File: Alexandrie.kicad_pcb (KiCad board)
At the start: 2 copper layers, 100 x 100 mm, 786 parts, among them J1 kk_10, J11 CONN_01X03, J2 kk_5, J3 kk_5, J4 CONN_01X06, J5 CONN_01X02, J6 CONN_01X13, J7 Conn_01x07, J8 kk_10, U1 74HCT04, U12 78M05 Dpak, U2 74HCT04, U3 TPIC6B595, U4 TPIC6B595, U6 TPIC6B595, U7 TPIC6B595

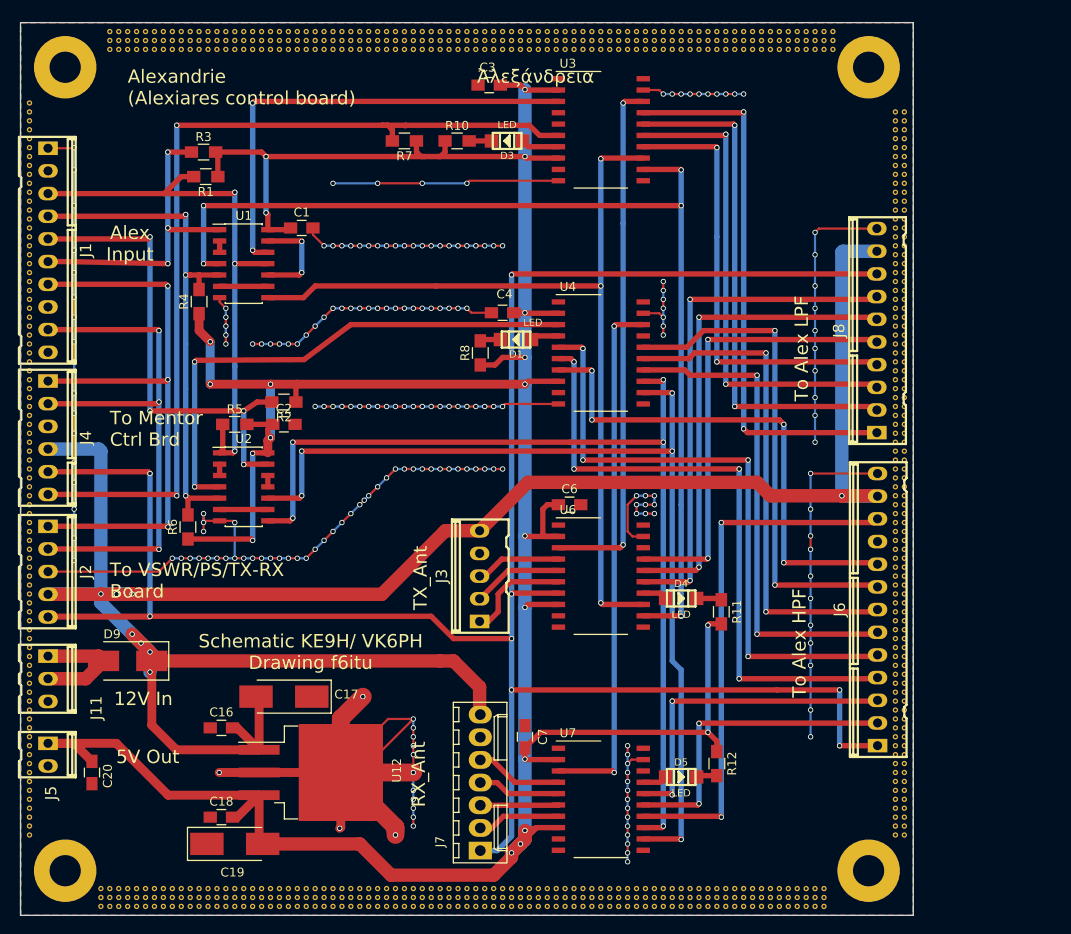
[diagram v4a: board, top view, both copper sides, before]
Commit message: upgrate to Kicad 5.0n, new up to date Gerber
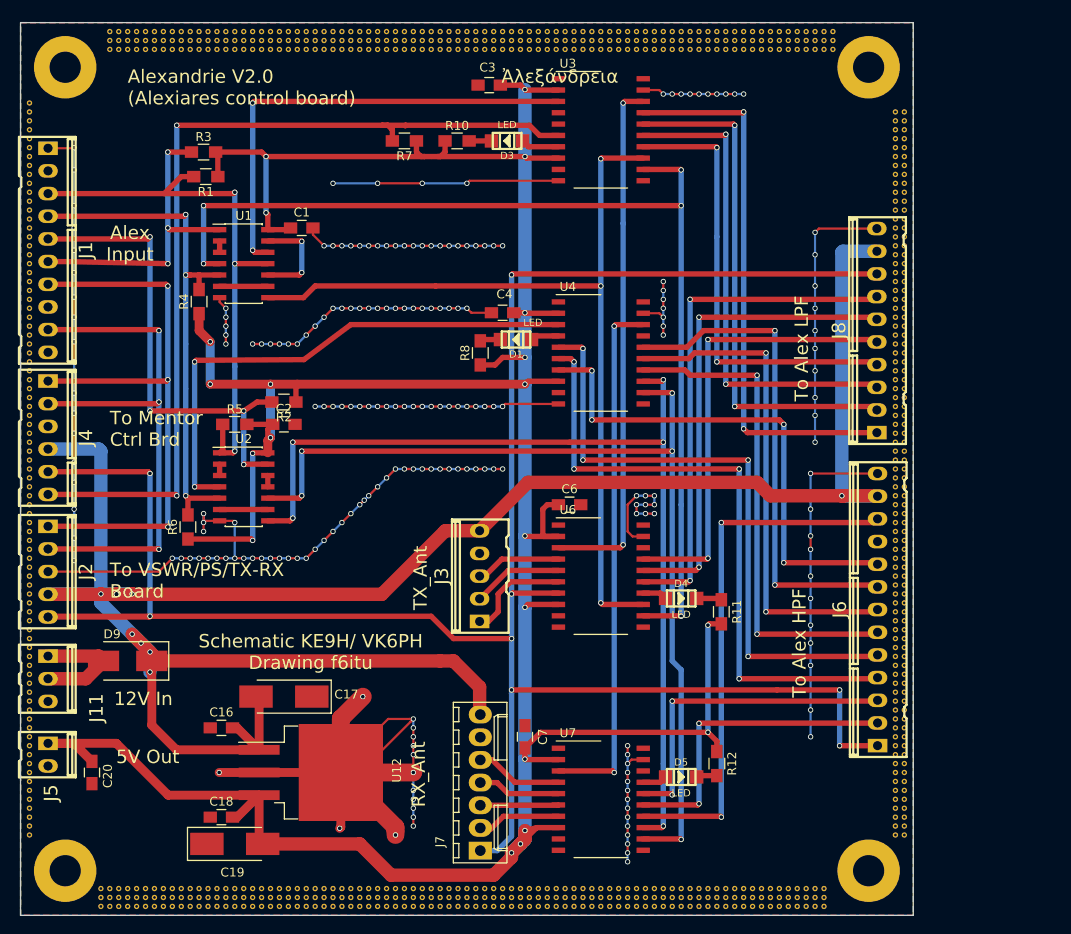
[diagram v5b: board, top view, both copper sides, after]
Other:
- board text added: "Alexandrie V2.0 Ἀλεξάνδρεια (Alexiares control board)"
- board text removed: "Alexandrie Ἀλεξάνδρεια (Alexiares control board)"
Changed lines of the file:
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@@
-(kicad_pcb (version 4) (host pcbnew 4.0.7)
+(kicad_pcb (version 20171130) (host pcbnew "(5.0.2)-1")
   (general
-    (links 902)
-    (no_connects 0)
-    (area 88.924999 42.924999 189.075001 143.075001)
     (thickness 1.6)
     (drawings 27)
@@
     (pad_drill 0.3)
     (pad_to_mask_clearance 0.2)
+    (solder_mask_min_width 0.25)
     (aux_axis_origin 0 0)
     (visible_elements 7FFFF77F)
     (pcbplotparams
-      (layerselection 0x010f0_80000001)
+      (layerselection 0x010f0_ffffffff)
       (usegerberextensions true)
-      (excludeedgelayer true)
+      (usegerberattributes true)
+      (usegerberadvancedattributes false)
+      (creategerberjobfile false)
+      (excludeedgelayer false)
       (linewidth 0.100000)
       (plotframeref false)
@@
       (hpglpennumber 1)
       (hpglpenspeed 20)
-      (hpglpendiameter 15)
-      (hpglpenoverlay 2)
+      (hpglpendiameter 15.000000)
       (psnegative false)
       (psa4output false)
@@
       (drillshape 0)
       (scaleselection 1)
-      (outputdirectory Gerber/))
+      (outputdirectory "Gerber/"))
   )
   (net 0 "")
@@
     (descr "10 pin vert. connector, Molex KK100 series")
     (fp_text reference J1 (at 0 -4.318 270) (layer F.SilkS)
-      (effects (font (thickness 0.3048)))
+      (effects (font (size 1.524 1.524) (thickness 0.3048)))
     )
     (fp_text value kk_10 (at 0 4.56946 270) (layer F.SilkS) hide
-      (effects (font (thickness 0.3048)))
+      (effects (font (size 1.524 1.524) (thickness 0.3048)))
     )
     (fp_line (start -2.286 -2.286) (end 12.446 -2.286) (layer F.SilkS) (width 0.254))
@@
     (descr "5 pin vert. connector, Molex KK100 series")
     (fp_text reference J2 (at 0 -4.318 270) (layer F.SilkS)
-      (effects (font (thickness 0.3048)))
+      (effects (font (size 1.524 1.524) (thickness 0.3048)))
     )
     (fp_text value kk_5 (at 0 4.56946 270) (layer F.SilkS) hide
-      (effects (font (thickness 0.3048)))
+      (effects (font (size 1.524 1.524) (thickness 0.3048)))
     )
     (fp_line (start 6.096 -2.794) (end -6.096 -2.794) (layer F.SilkS) (width 0.254))
@@
     (descr "6 pin vert. connector, Molex KK100 series")
     (fp_text reference J4 (at 0 -4.318 270) (layer F.SilkS)
-      (effects (font (thickness 0.3048)))
+      (effects (font (size 1.524 1.524) (thickness 0.3048)))
     )
     (fp_text value CONN_01X06 (at 0 4.56946 270) (layer F.SilkS) hide
-      (effects (font (thickness 0.3048)))
+      (effects (font (size 1.524 1.524) (thickness 0.3048)))
     )
     (fp_line (start 2.794 -2.286) (end 7.366 -2.286) (layer F.SilkS) (width 0.254))
@@
     (descr "2 pin vert. connector, Molex KK100 series")
     (fp_text reference J5 (at 4.3 -0.415 270) (layer F.SilkS)
-      (effects (font (thickness 0.3048)))
+      (effects (font (size 1.524 1.524) (thickness 0.3048)))
     )
     (fp_text value CONN_01X02 (at 0 4.572 270) (layer F.SilkS) hide
-      (effects (font (thickness 0.3048)))
+      (effects (font (size 1.524 1.524) (thickness 0.3048)))
     )
     (fp_line (start -2.286 -2.286) (end 2.286 -2.286) (layer F.SilkS) (width 0.254))
@@
     (descr "10 pin vert. connector, Molex KK100 series")
     (fp_text reference J8 (at 0 -4.318 90) (layer F.SilkS)
-      (effects (font (thickness 0.3048)))
+      (effects (font (size 1.524 1.524) (thickness 0.3048)))
     )
     (fp_text value kk_10 (at 0 4.56946 90) (layer F.SilkS) hide
-      (effects (font (thickness 0.3048)))
+      (effects (font (size 1.524 1.524) (thickness 0.3048)))
     )
     (fp_line (start -2.286 -2.286) (end 12.446 -2.286) (layer F.SilkS) (width 0.254))
@@
     (descr "3 pin vert. connector, Molex KK100 series")
     (fp_text reference J11 (at 3.275 -5.495 270) (layer F.SilkS)
-      (effects (font (thickness 0.3048)))
+      (effects (font (size 1.524 1.524) (thickness 0.3048)))
     )
     (fp_text value CONN_01X03 (at 0 4.56946 270) (layer F.SilkS) hide
-      (effects (font (thickness 0.3048)))
+      (effects (font (size 1.524 1.524) (thickness 0.3048)))
     )
     (fp_line (start -3.556 -2.286) (end 3.556 -2.286) (layer F.SilkS) (width 0.254))
@@
       (net 2 GND))
     (model TO_SOT_Packages_SMD.3dshapes/TO-263-3Lead.wrl
-      (at (xyz -0.2 0 0))
+      (offset (xyz -5.079999923706055 0 0))
       (scale (xyz 1 1 1))
       (rotate (xyz 0 0 90))
@@
     (descr "5 pin vert. connector, Molex KK100 series")
     (fp_text reference J3 (at 0 -4.318 90) (layer F.SilkS)
-      (effects (font (thickness 0.3048)))
+      (effects (font (size 1.524 1.524) (thickness 0.3048)))
     )
     (fp_text value kk_5 (at 0 4.56946 90) (layer F.SilkS) hide
-      (effects (font (thickness 0.3048)))
+      (effects (font (size 1.524 1.524) (thickness 0.3048)))
     )
     (fp_line (start 6.096 -2.794) (end -6.096 -2.794) (layer F.SilkS) (width 0.254))
@@
     (descr "13 pin vert. connector, Molex KK100 series")
     (fp_text reference J6 (at 0 -4.318 90) (layer F.SilkS)
-      (effects (font (thickness 0.3048)))
+      (effects (font (size 1.524 1.524) (thickness 0.3048)))
     )
     (fp_text value CONN_01X13 (at 0 4.56946 90) (layer F.SilkS) hide
-      (effects (font (thickness 0.3048)))
+      (effects (font (size 1.524 1.524) (thickness 0.3048)))
     )
     (fp_line (start 4.064 -2.794) (end 16.256 -2.794) (layer F.SilkS) (width 0.254))
@@
       (net 18 +12V))
     (model ${KISYS3DMOD}/Connectors_Molex.3dshapes/Molex_KK-6410-07_07x2.54mm_Straight.wrl
-      (at (xyz 0.6 0 0))
+      (offset (xyz 15.23999977111816 0 0))
       (scale (xyz 1 1 1))
       (rotate (xyz 0 0 180))
@@
     (effects (font (size 1.5 1.5) (thickness 0.3)) (justify left mirror))
   )
-  (gr_text "Alexandrie                                           Ἀλεξάνδρεια \n(Alexiares control board)\n" (at 101 50.25) (layer F.SilkS)
+  (gr_text "Alexandrie V2.0                                       Ἀλεξάνδρεια \n(Alexiares control board)\n" (at 101 50.25) (layer F.SilkS)
     (effects (font (size 1.5 1.5) (thickness 0.3)) (justify left))
   )

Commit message: cleaning, new bom and interactive bom
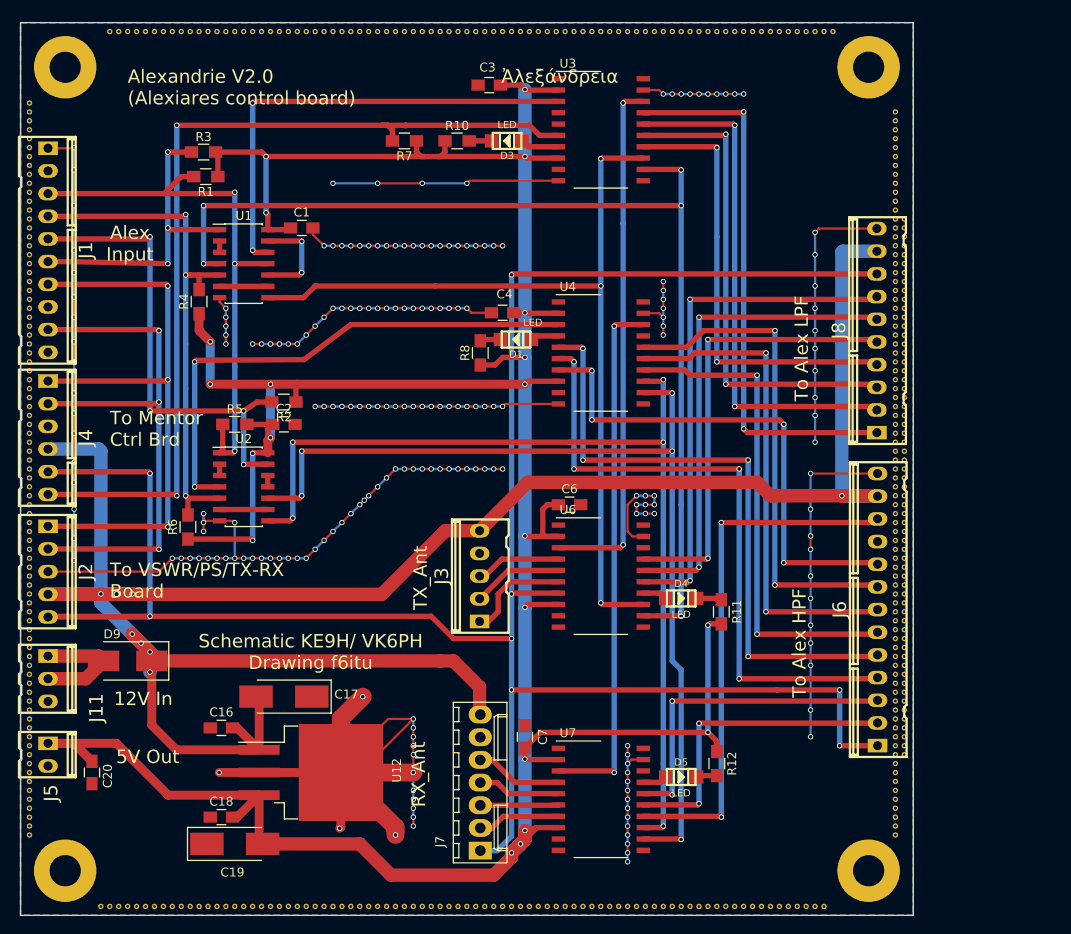
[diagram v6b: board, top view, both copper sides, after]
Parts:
- removed the REF** at (179.0, 141.0)
- removed the REF** at (178.0, 141.0)
- removed the REF** at (177.0, 141.0)
- removed the REF** at (176.0, 141.0)
- removed the REF** at (175.0, 141.0)
- removed the REF** at (174.0, 141.0)
- removed the REF** at (173.0, 141.0)
- removed the REF** at (172.0, 141.0)
- removed the REF** at (171.0, 141.0)
- removed the REF** at (170.0, 141.0)
- removed the REF** at (169.0, 141.0)
- removed the REF** at (168.0, 141.0)
- removed the REF** at (167.0, 141.0)
- removed the REF** at (166.0, 141.0)
- removed the REF** at (165.0, 141.0)
- removed the REF** at (164.0, 141.0)
- removed the REF** at (163.0, 141.0)
- removed the REF** at (162.0, 141.0)
- removed the REF** at (161.0, 141.0)
- removed the REF** at (160.0, 141.0)
- removed the REF** at (159.0, 141.0)
- removed the REF** at (158.0, 141.0)
- removed the REF** at (157.0, 141.0)
- removed the REF** at (156.0, 141.0)
- removed the REF** at (155.0, 141.0)
- removed the REF** at (154.0, 141.0)
- removed the REF** at (153.0, 141.0)
- removed the REF** at (152.0, 141.0)
- removed the REF** at (151.0, 141.0)
- removed the REF** at (150.0, 141.0)
- removed the REF** at (149.0, 141.0)
- removed the REF** at (148.0, 141.0)
- removed the REF** at (147.0, 141.0)
- removed the REF** at (146.0, 141.0)
- removed the REF** at (145.0, 141.0)
- removed the REF** at (144.0, 141.0)
- removed the REF** at (143.0, 141.0)
- removed the REF** at (142.0, 141.0)
- removed the REF** at (141.0, 141.0)
- removed the REF** at (140.0, 141.0)
- removed the REF** at (139.0, 141.0)
- removed the REF** at (138.0, 141.0)
- removed the REF** at (137.0, 141.0)
- removed the REF** at (136.0, 141.0)
- removed the REF** at (135.0, 141.0)
- removed the REF** at (134.0, 141.0)
- removed the REF** at (133.0, 141.0)
- removed the REF** at (132.0, 141.0)
- removed the REF** at (131.0, 141.0)
- removed the REF** at (130.0, 141.0)
- removed the REF** at (129.0, 141.0)
- removed the REF** at (128.0, 141.0)
- removed the REF** at (127.0, 141.0)
- removed the REF** at (126.0, 141.0)
- removed the REF** at (125.0, 141.0)
- removed the REF** at (124.0, 141.0)
- removed the REF** at (123.0, 141.0)
- removed the REF** at (122.0, 141.0)
- removed the REF** at (121.0, 141.0)
- removed the REF** at (120.0, 141.0)
- removed the REF** at (119.0, 141.0)
- removed the REF** at (118.0, 141.0)
- removed the REF** at (117.0, 141.0)
- removed the REF** at (116.0, 141.0)
- removed the REF** at (115.0, 141.0)
- removed the REF** at (114.0, 141.0)
- removed the REF** at (113.0, 141.0)
- removed the REF** at (112.0, 141.0)
- removed the REF** at (111.0, 141.0)
- removed the REF** at (110.0, 141.0)
- removed the REF** at (109.0, 141.0)
- removed the REF** at (108.0, 141.0)
- removed the REF** at (107.0, 141.0)
- removed the REF** at (106.0, 141.0)
- removed the REF** at (105.0, 141.0)
- removed the REF** at (104.0, 141.0)
- removed the REF** at (103.0, 141.0)
- removed the REF** at (102.0, 141.0)
- removed the REF** at (101.0, 141.0)
- removed the REF** at (100.0, 141.0)
- removed the REF** at (99.0, 141.0)
- removed the REF** at (98.0, 141.0)
- removed the REF** at (179.0, 140.0)
- removed the REF** at (178.0, 140.0)
- removed the REF** at (177.0, 140.0)
- removed the REF** at (176.0, 140.0)
- removed the REF** at (175.0, 140.0)
- removed the REF** at (174.0, 140.0)
- removed the REF** at (173.0, 140.0)
- removed the REF** at (172.0, 140.0)
- removed the REF** at (171.0, 140.0)
- removed the REF** at (170.0, 140.0)
- removed the REF** at (169.0, 140.0)
- removed the REF** at (168.0, 140.0)
- removed the REF** at (167.0, 140.0)
- removed the REF** at (166.0, 140.0)
- removed the REF** at (165.0, 140.0)
- removed the REF** at (164.0, 140.0)
- removed the REF** at (163.0, 140.0)
- removed the REF** at (162.0, 140.0)
- removed the REF** at (161.0, 140.0)
- removed the REF** at (160.0, 140.0)
- removed the REF** at (159.0, 140.0)
- removed the REF** at (158.0, 140.0)
- removed the REF** at (157.0, 140.0)
- removed the REF** at (156.0, 140.0)
- removed the REF** at (155.0, 140.0)
- removed the REF** at (154.0, 140.0)
- removed the REF** at (153.0, 140.0)
- removed the REF** at (152.0, 140.0)
- removed the REF** at (151.0, 140.0)
- removed the REF** at (150.0, 140.0)
- removed the REF** at (149.0, 140.0)
- removed the REF** at (148.0, 140.0)
- removed the REF** at (147.0, 140.0)
- removed the REF** at (146.0, 140.0)
- removed the REF** at (145.0, 140.0)
- removed the REF** at (144.0, 140.0)
- removed the REF** at (143.0, 140.0)
- removed the REF** at (142.0, 140.0)
- removed the REF** at (141.0, 140.0)
- removed the REF** at (140.0, 140.0)
- removed the REF** at (139.0, 140.0)
- removed the REF** at (138.0, 140.0)
- removed the REF** at (137.0, 140.0)
- removed the REF** at (136.0, 140.0)
- removed the REF** at (135.0, 140.0)
- removed the REF** at (134.0, 140.0)
- removed the REF** at (133.0, 140.0)
- removed the REF** at (132.0, 140.0)
- removed the REF** at (131.0, 140.0)
- removed the REF** at (130.0, 140.0)
- removed the REF** at (129.0, 140.0)
- removed the REF** at (128.0, 140.0)
- removed the REF** at (127.0, 140.0)
- removed the REF** at (126.0, 140.0)
- removed the REF** at (125.0, 140.0)
- removed the REF** at (124.0, 140.0)
- removed the REF** at (123.0, 140.0)
- removed the REF** at (122.0, 140.0)
- removed the REF** at (121.0, 140.0)
- removed the REF** at (120.0, 140.0)
- removed the REF** at (119.0, 140.0)
- removed the REF** at (118.0, 140.0)
- removed the REF** at (117.0, 140.0)
- removed the REF** at (116.0, 140.0)
- removed the REF** at (115.0, 140.0)
- removed the REF** at (114.0, 140.0)
- removed the REF** at (113.0, 140.0)
- removed the REF** at (112.0, 140.0)
- removed the REF** at (111.0, 140.0)
- removed the REF** at (110.0, 140.0)
- removed the REF** at (109.0, 140.0)
- removed the REF** at (108.0, 140.0)
- removed the REF** at (107.0, 140.0)
- removed the REF** at (106.0, 140.0)
- removed the REF** at (105.0, 140.0)
- removed the REF** at (104.0, 140.0)
- removed the REF** at (103.0, 140.0)
- removed the REF** at (102.0, 140.0)
- removed the REF** at (101.0, 140.0)
- removed the REF** at (100.0, 140.0)
- removed the REF** at (99.0, 140.0)
- removed the REF** at (98.0, 140.0)
- removed the REF** at (188.0, 134.0)
- removed the REF** at (188.0, 133.0)
- removed the REF** at (188.0, 132.0)
- removed the REF** at (188.0, 131.0)
- removed the REF** at (188.0, 130.0)
- removed the REF** at (188.0, 129.0)
- removed the REF** at (188.0, 128.0)
- removed the REF** at (188.0, 127.0)
- removed the REF** at (188.0, 126.0)
- removed the REF** at (188.0, 64.0)
- removed the REF** at (188.0, 63.0)
- removed the REF** at (188.0, 62.0)
- removed the REF** at (188.0, 61.0)
- removed the REF** at (188.0, 60.0)
- removed the REF** at (188.0, 59.0)
- removed the REF** at (188.0, 58.0)
- removed the REF** at (188.0, 57.0)
- removed the REF** at (188.0, 56.0)
- removed the REF** at (188.0, 55.0)
- removed the REF** at (188.0, 54.0)
- removed the REF** at (188.0, 53.0)
- removed the REF** at (180.0, 46.0)
- removed the REF** at (179.0, 46.0)
- removed the REF** at (178.0, 46.0)
- removed the REF** at (177.0, 46.0)
- removed the REF** at (176.0, 46.0)
- removed the REF** at (175.0, 46.0)
- removed the REF** at (174.0, 46.0)
- removed the REF** at (173.0, 46.0)
- removed the REF** at (172.0, 46.0)
- removed the REF** at (171.0, 46.0)
- removed the REF** at (170.0, 46.0)
- removed the REF** at (169.0, 46.0)
- removed the REF** at (168.0, 46.0)
- removed the REF** at (167.0, 46.0)
- removed the REF** at (166.0, 46.0)
- removed the REF** at (165.0, 46.0)
- removed the REF** at (164.0, 46.0)
- removed the REF** at (163.0, 46.0)
- removed the REF** at (162.0, 46.0)
- removed the REF** at (161.0, 46.0)
- removed the REF** at (160.0, 46.0)
- removed the REF** at (159.0, 46.0)
- removed the REF** at (158.0, 46.0)
- removed the REF** at (157.0, 46.0)
- removed the REF** at (156.0, 46.0)
- removed the REF** at (155.0, 46.0)
- removed the REF** at (154.0, 46.0)
- removed the REF** at (153.0, 46.0)
- removed the REF** at (152.0, 46.0)
- removed the REF** at (151.0, 46.0)
- removed the REF** at (150.0, 46.0)
- removed the REF** at (149.0, 46.0)
- removed the REF** at (148.0, 46.0)
- removed the REF** at (147.0, 46.0)
- removed the REF** at (146.0, 46.0)
- removed the REF** at (145.0, 46.0)
- removed the REF** at (144.0, 46.0)
- removed the REF** at (143.0, 46.0)
- removed the REF** at (142.0, 46.0)
- removed the REF** at (141.0, 46.0)
- removed the REF** at (140.0, 46.0)
- removed the REF** at (139.0, 46.0)
- removed the REF** at (138.0, 46.0)
- removed the REF** at (137.0, 46.0)
- removed the REF** at (136.0, 46.0)
- removed the REF** at (135.0, 46.0)
- removed the REF** at (134.0, 46.0)
- removed the REF** at (133.0, 46.0)
- removed the REF** at (132.0, 46.0)
- removed the REF** at (131.0, 46.0)
- removed the REF** at (130.0, 46.0)
- removed the REF** at (129.0, 46.0)
- removed the REF** at (128.0, 46.0)
- removed the REF** at (127.0, 46.0)
- removed the REF** at (126.0, 46.0)
- removed the REF** at (125.0, 46.0)
- removed the REF** at (124.0, 46.0)
- removed the REF** at (123.0, 46.0)
- removed the REF** at (122.0, 46.0)
- removed the REF** at (121.0, 46.0)
- removed the REF** at (120.0, 46.0)
- removed the REF** at (119.0, 46.0)
- removed the REF** at (118.0, 46.0)
- removed the REF** at (117.0, 46.0)
- removed the REF** at (116.0, 46.0)
- removed the REF** at (115.0, 46.0)
- removed the REF** at (114.0, 46.0)
- removed the REF** at (113.0, 46.0)
- removed the REF** at (112.0, 46.0)
- removed the REF** at (111.0, 46.0)
- removed the REF** at (110.0, 46.0)
- removed the REF** at (109.0, 46.0)
- removed the REF** at (108.0, 46.0)
- removed the REF** at (107.0, 46.0)
- removed the REF** at (106.0, 46.0)
- removed the REF** at (105.0, 46.0)
- removed the REF** at (104.0, 46.0)
- removed the REF** at (103.0, 46.0)
- removed the REF** at (102.0, 46.0)
- removed the REF** at (101.0, 46.0)
- removed the REF** at (100.0, 46.0)
- removed the REF** at (99.0, 46.0)
- removed the REF** at (180.0, 45.0)
- removed the REF** at (179.0, 45.0)
- removed the REF** at (178.0, 45.0)
- removed the REF** at (177.0, 45.0)
- removed the REF** at (176.0, 45.0)
- removed the REF** at (175.0, 45.0)
- removed the REF** at (174.0, 45.0)
- removed the REF** at (173.0, 45.0)
- removed the REF** at (172.0, 45.0)
- removed the REF** at (171.0, 45.0)
- removed the REF** at (170.0, 45.0)
- removed the REF** at (169.0, 45.0)
- removed the REF** at (168.0, 45.0)
- removed the REF** at (167.0, 45.0)
- removed the REF** at (166.0, 45.0)
- removed the REF** at (165.0, 45.0)
- removed the REF** at (164.0, 45.0)
- removed the REF** at (163.0, 45.0)
- removed the REF** at (162.0, 45.0)
- removed the REF** at (161.0, 45.0)
- removed the REF** at (160.0, 45.0)
- removed the REF** at (159.0, 45.0)
- removed the REF** at (158.0, 45.0)
- removed the REF** at (157.0, 45.0)
- removed the REF** at (156.0, 45.0)
- removed the REF** at (155.0, 45.0)
- removed the REF** at (154.0, 45.0)
- removed the REF** at (153.0, 45.0)
- removed the REF** at (152.0, 45.0)
- removed the REF** at (151.0, 45.0)
- removed the REF** at (150.0, 45.0)
- removed the REF** at (149.0, 45.0)
- removed the REF** at (148.0, 45.0)
- removed the REF** at (147.0, 45.0)
- removed the REF** at (146.0, 45.0)
- removed the REF** at (145.0, 45.0)
- removed the REF** at (144.0, 45.0)
- removed the REF** at (143.0, 45.0)
- removed the REF** at (142.0, 45.0)
- removed the REF** at (141.0, 45.0)
- removed the REF** at (140.0, 45.0)
- removed the REF** at (139.0, 45.0)
- removed the REF** at (138.0, 45.0)
- removed the REF** at (137.0, 45.0)
- removed the REF** at (136.0, 45.0)
- removed the REF** at (135.0, 45.0)
- removed the REF** at (134.0, 45.0)
- removed the REF** at (133.0, 45.0)
- removed the REF** at (132.0, 45.0)
- removed the REF** at (131.0, 45.0)
- removed the REF** at (130.0, 45.0)
- removed the REF** at (129.0, 45.0)
- removed the REF** at (128.0, 45.0)
- removed the REF** at (127.0, 45.0)
- removed the REF** at (126.0, 45.0)
- removed the REF** at (125.0, 45.0)
- removed the REF** at (124.0, 45.0)
- removed the REF** at (123.0, 45.0)
- removed the REF** at (122.0, 45.0)
- removed the REF** at (121.0, 45.0)
- removed the REF** at (120.0, 45.0)
- removed the REF** at (119.0, 45.0)
- removed the REF** at (118.0, 45.0)
- removed the REF** at (117.0, 45.0)
- removed the REF** at (116.0, 45.0)
- removed the REF** at (115.0, 45.0)
- removed the REF** at (114.0, 45.0)
- removed the REF** at (113.0, 45.0)
- removed the REF** at (112.0, 45.0)
- removed the REF** at (111.0, 45.0)
- removed the REF** at (110.0, 45.0)
- removed the REF** at (109.0, 45.0)
- removed the REF** at (108.0, 45.0)
- removed the REF** at (107.0, 45.0)
- removed the REF** at (106.0, 45.0)
- removed the REF** at (105.0, 45.0)
- removed the REF** at (104.0, 45.0)
- removed the REF** at (103.0, 45.0)
- removed the REF** at (102.0, 45.0)
- removed the REF** at (101.0, 45.0)
- removed the REF** at (100.0, 45.0)
- removed the REF** at (99.0, 45.0)

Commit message: last commit, project deprecated, replaced by AlexV2
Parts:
- removed REF** (x390): via, via:via
- C1, C16, C18, C2, C20, C3, C4, C6, C7: footprint Capacitors_SMD:C_0805_HandSoldering -> Capacitor_SMD:C_0805_2012Metric_Pad1.18x1.45mm_HandSolder
- D1, D3, D4, D5: footprint smd_leds:Led_1206 -> LED_SMD:LED_1206_3216Metric_Pad1.42x1.75mm_HandSolder
- R1, R10, R11, R12, R2, R3, R4, R5, R6, R7, R8: footprint Resistors_SMD:R_0805_HandSoldering -> Resistor_SMD:R_0805_2012Metric_Pad1.20x1.40mm_HandSolder
- U1, U2: footprint Housings_SOIC:SOIC-14_3.9x8.7mm_Pitch1.27mm -> Package_SO:SO-14_3.9x8.65mm_P1.27mm
- U3, U4, U6, U7: footprint Housings_SOIC:SO-20_12.8x7.5mm_Pitch1.27mm -> Package_SO:SO-20_12.8x7.5mm_P1.27mm
- turned C17 to 0 degrees
- turned C19 to 180 degrees
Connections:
- net 12/10m renamed 12/10m
- net 17/15m renamed 17/15m
- net 30/20m renamed 30/20m
- C17 pad 1: GND -> +12V
- C17 pad 2: +12V -> GND
- C19 pad 1: GND -> +5V
- C19 pad 2: +5V -> GND
- J1 pad 2: (no net) -> unconnected-(J1-Pad2)
- J1 pad 8: (no net) -> unconnected-(J1-Pad8)
- U3 pad 1: (no net) -> unconnected-(U3-Pad1)
- U3 pad 20: (no net) -> unconnected-(U3-Pad20)
- U3 pad 4: (no net) -> unconnected-(U3-Pad4)
- U3 pad 5: (no net) -> unconnected-(U3-Pad5)
- U4 pad 1: (no net) -> +5V
- U4 pad 17: (no net) -> unconnected-(U4-Pad17)
- U4 pad 2: +5V -> Net-(U4-Pad2)
- U4 pad 20: (no net) -> unconnected-(U4-Pad20)
- U4 pad 8: +5V -> Net-(U4-Pad2)
- U6 pad 1: (no net) -> +5V
- U6 pad 18: (no net) -> unconnected-(U6-Pad18)
- U6 pad 2: +5V -> unconnected-(U6-Pad2)
- U6 pad 20: (no net) -> unconnected-(U6-Pad20)
- U7 pad 1: (no net) -> +5V
- U7 pad 18: (no net) -> unconnected-(U7-Pad18)
- U7 pad 2: +5V -> Net-(U7-Pad2)
- U7 pad 20: (no net) -> unconnected-(U7-Pad20)
- U7 pad 8: +5V -> Net-(U7-Pad2)
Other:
- net class Default removed
